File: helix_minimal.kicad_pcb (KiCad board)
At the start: 2 copper layers, 50 x 50 mm, 20 parts, among them J1 USB-C, J4 sd card, J5 SWD, J6 pico hdmi, U1 STM32C071FBP6, U2 AP2112K-3.3, U3 WIZ850io

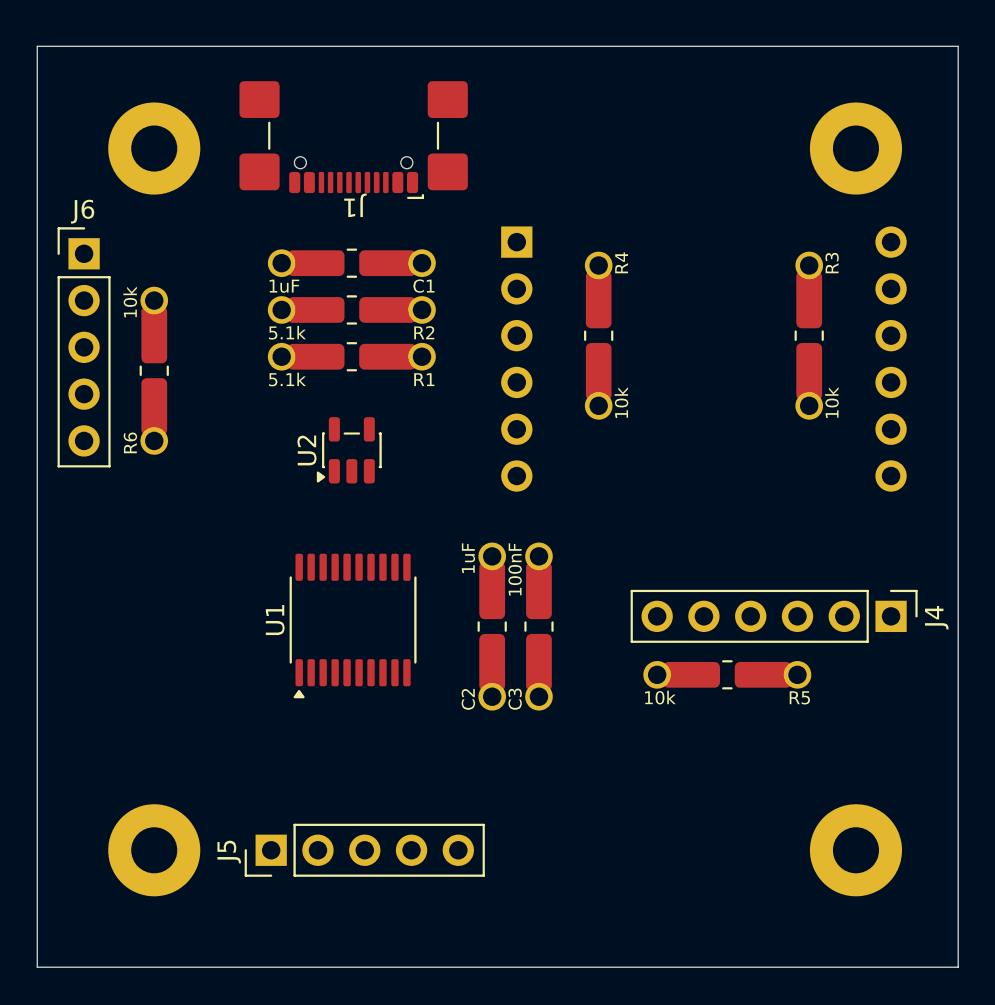
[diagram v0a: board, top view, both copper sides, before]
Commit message: Route PCB with fixed fine-pitch rules
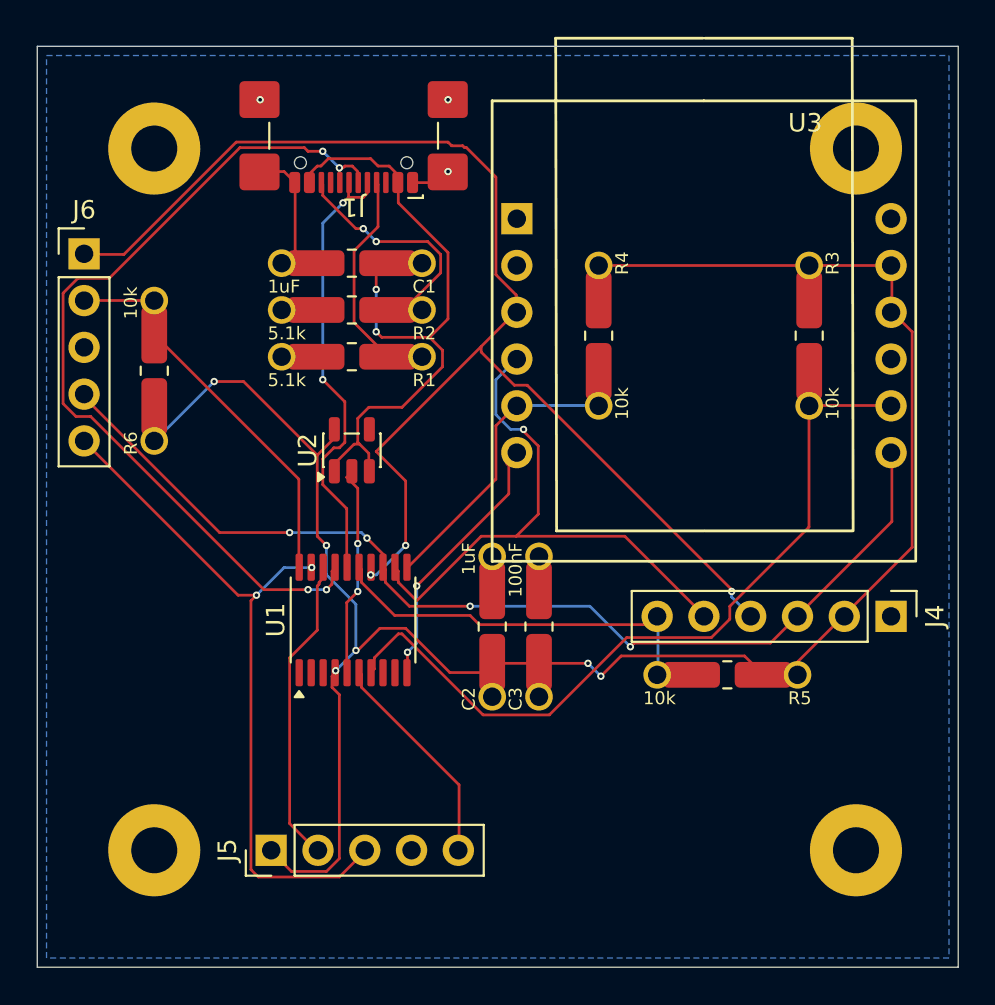
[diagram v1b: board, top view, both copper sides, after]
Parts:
- moved U3 1.27 mm to (137.8, 73.7)
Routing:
- net +3V3: track 0.00 -> 107.7 mm, vias 0 -> 6
- net /SPI_MOSI: track 0.00 -> 73.9 mm, vias 0 -> 3
- net /SPI_MISO: track 0.00 -> 57.0 mm, vias 0 -> 4
- net /USB_DP: track 0.00 -> 46.5 mm, vias 0 -> 4
- net /WIZ_RST: track 0.00 -> 42.6 mm
- net /SWCLK: track 0.00 -> 38.5 mm, vias 0 -> 2
- net VBUS: track 0.00 -> 36.5 mm, vias 0 -> 2
- net /SPI_SCK: track 0.00 -> 33.0 mm, vias 0 -> 1
- net /USB_DM: track 0.00 -> 24.9 mm, vias 0 -> 2
- net /SD_CS: track 0.00 -> 21.3 mm
- net GND: track 0.00 -> 20.8 mm, vias 0 -> 5
- net /PICO_CS: track 0.00 -> 19.8 mm
- net /SWDIO: track 0.00 -> 16.0 mm
- net /WIZ_CS: track 0.00 -> 15.8 mm
- net /WIZ_INT: track 0.00 -> 14.3 mm, vias 0 -> 2
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- added copper zone on B.Cu, net GND

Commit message: Reroute PCB without in-pad vias and widen copper
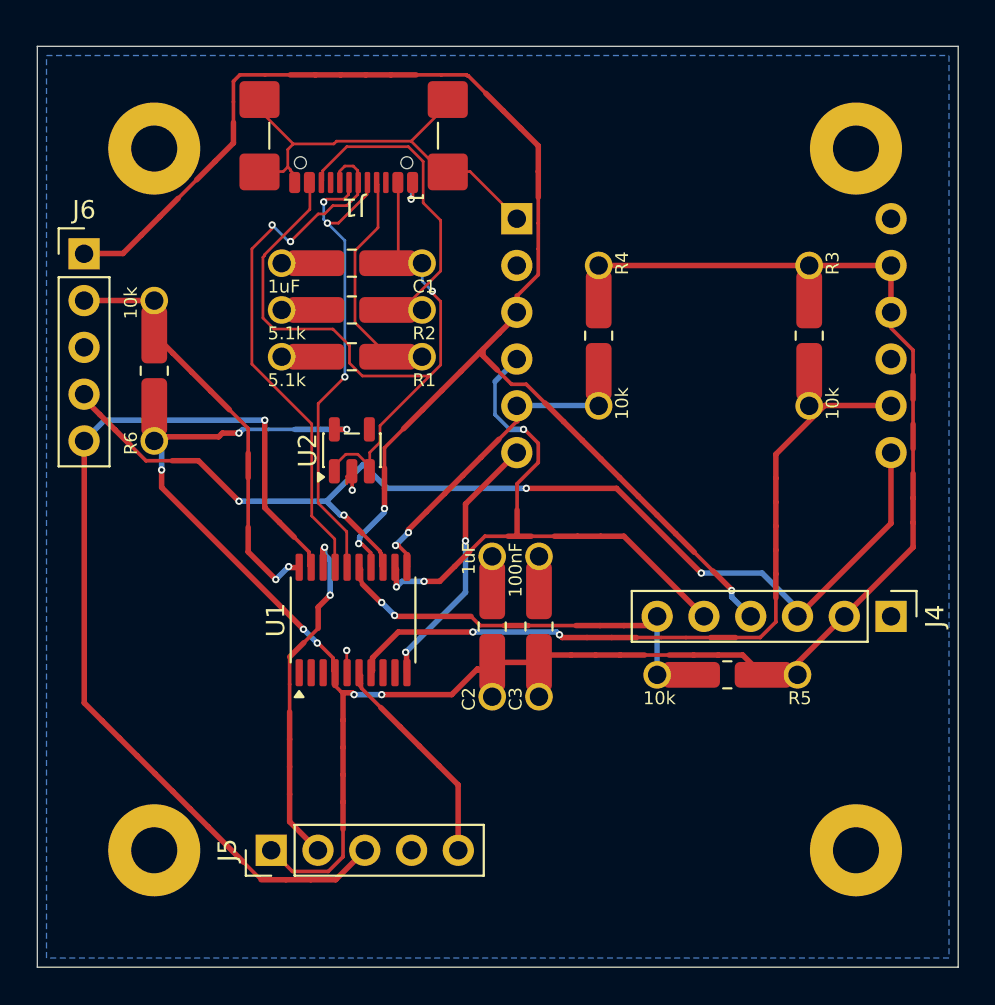
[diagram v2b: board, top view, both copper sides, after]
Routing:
- net /USB_DP: track 46.5 -> 29.4 mm, vias 4 -> 2
- net /SWCLK: track 38.5 -> 53.4 mm, vias 2 -> 1
- net GND: track 20.8 -> 29.6 mm, vias 5 -> 3
- net /SPI_MOSI: track 73.9 -> 80.0 mm
- net VBUS: track 36.5 -> 41.6 mm, vias 2 -> 1
- net /SPI_MISO: track 57.0 -> 61.1 mm
- net /CC2: track 13.3 -> 17.1 mm, vias 2 -> 0
- net /SWDIO: track 16.0 -> 19.3 mm, vias 0 -> 2
- net /USB_DM: track 24.9 -> 27.2 mm, vias 2 -> 3
- net /WIZ_RST: track 42.6 -> 40.9 mm, vias 0 -> 2
- net /PICO_CS: track 19.8 -> 21.3 mm, vias 0 -> 2
- net /WIZ_CS: track 15.8 -> 16.4 mm, vias 0 -> 2
- net /SPI_SCK: track 33.0 -> 32.7 mm, vias 1 -> 3
- net /SD_CS: track 21.3 -> 21.2 mm, vias 0 -> 2
- net +3V3: track 107.7 -> 107.5 mm, vias 6 -> 7

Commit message: Reroute board with hard 0.30 mm ordinary traces
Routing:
- net GND: track 29.6 -> 181.3 mm, vias 3 -> 7
- net /SWCLK: track 53.4 -> 32.9 mm, vias 1 -> 0
- net VBUS: track 41.6 -> 30.4 mm
- net /SPI_MOSI: track 80.0 -> 68.9 mm, vias 3 -> 2
- net /SWDIO: track 19.3 -> 29.7 mm, vias 2 -> 0
- net /USB_DM: track 27.2 -> 34.2 mm
- net /CC2: track 17.1 -> 10.6 mm, vias 0 -> 2
- net /WIZ_RST: track 40.9 -> 35.1 mm
- net +3V3: track 107.5 -> 104.3 mm, vias 7 -> 5
- net /SPI_SCK: track 32.7 -> 34.8 mm, vias 3 -> 0
- net /USB_DP: track 29.4 -> 27.5 mm
- net /SPI_MISO: track 61.1 -> 62.6 mm, vias 4 -> 7
- net /PICO_CS: track 21.3 -> 20.1 mm, vias 2 -> 0
- net /SD_CS: track 21.2 -> 21.9 mm, vias 2 -> 1
- net /WIZ_CS: track 16.4 -> 15.7 mm, vias 2 -> 0
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
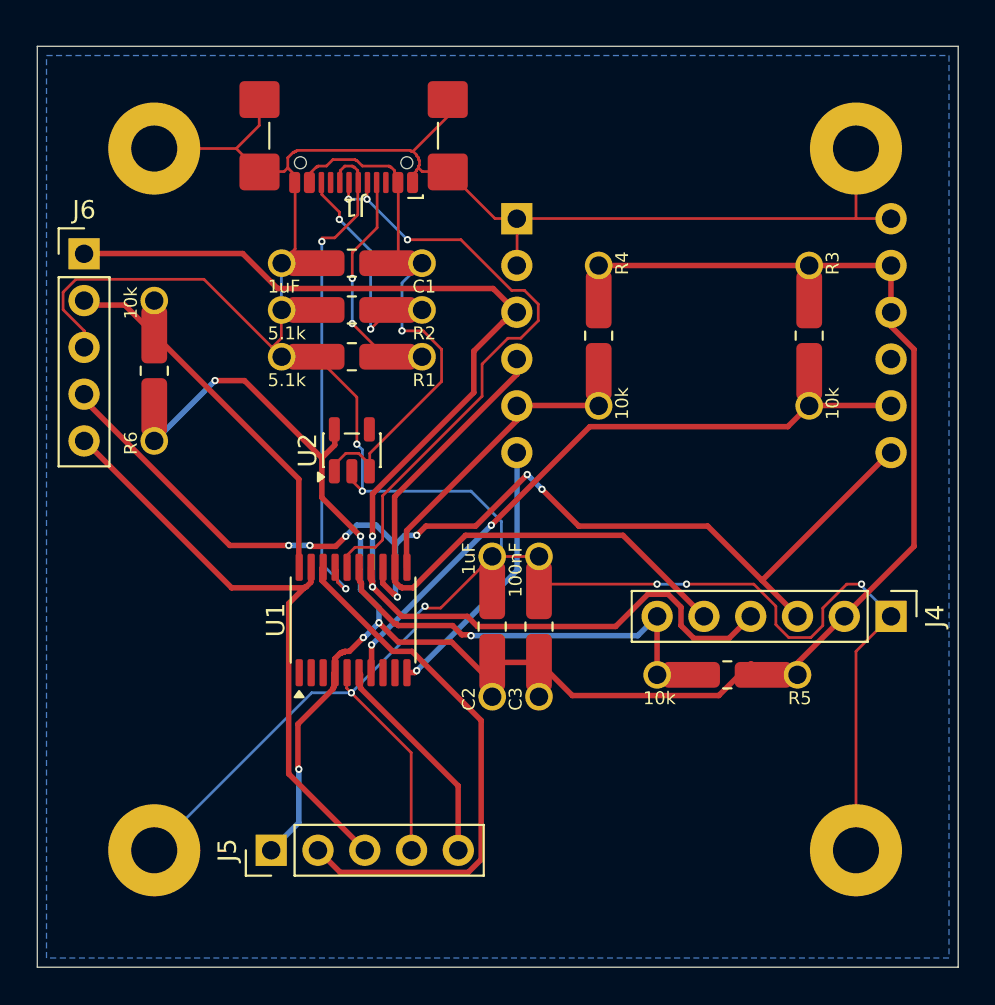
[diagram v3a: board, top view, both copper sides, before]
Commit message: Use dual ground pours and route signals with higher via cost
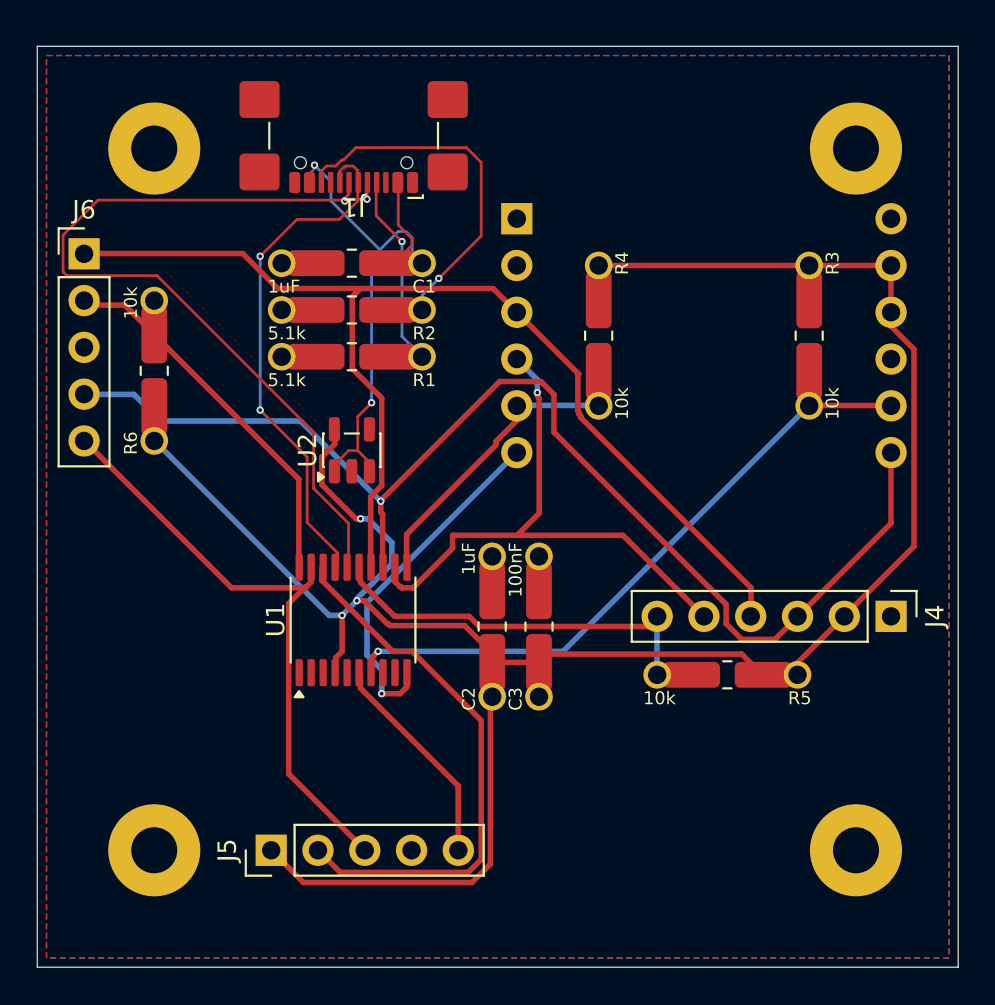
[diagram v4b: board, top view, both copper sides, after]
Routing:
- net GND: track 181.3 -> 0.00 mm, vias 7 -> 0
- net +3V3: track 104.3 -> 120.6 mm, vias 5 -> 3
- net /USB_DM: track 34.2 -> 46.8 mm, vias 3 -> 2
- net /CC2: track 10.6 -> 21.4 mm, vias 2 -> 1
- net /SPI_MOSI: track 68.9 -> 62.9 mm, vias 2 -> 0
- net /WIZ_INT: track 14.7 -> 19.1 mm
- net /SPI_MISO: track 62.6 -> 66.6 mm, vias 7 -> 1
- net /SPI_SCK: track 34.8 -> 31.5 mm, vias 0 -> 1
- net VBUS: track 30.4 -> 32.5 mm, vias 1 -> 2
- net /CC1: track 11.0 -> 12.4 mm, vias 2 -> 1
- net /USB_DP: track 27.5 -> 28.1 mm
- net /SD_CS: track 21.9 -> 21.4 mm, vias 1 -> 0
- net /WIZ_RST: track 35.1 -> 34.7 mm, vias 2 -> 1
- added copper zone on F.Cu, net GND

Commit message: Increase router turn penalty and reroute signal copper
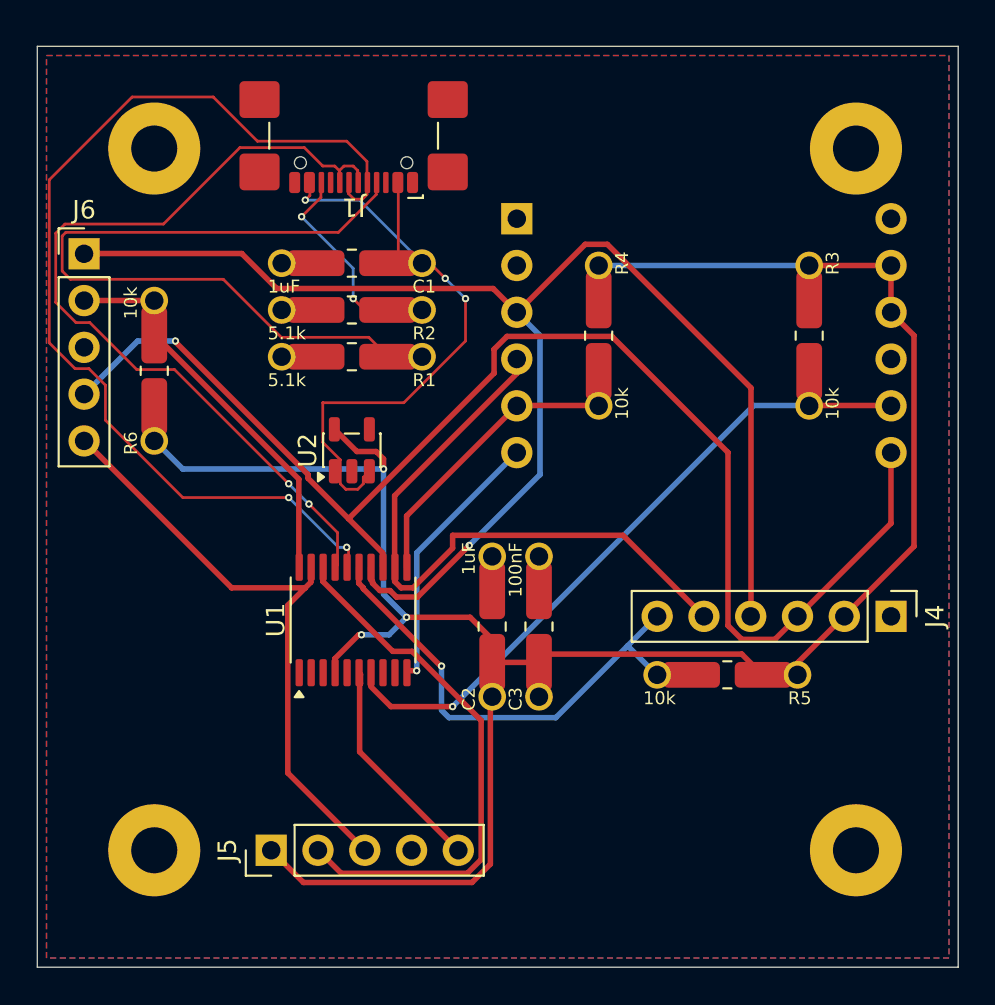
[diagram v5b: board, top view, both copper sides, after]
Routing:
- net /CC1: track 12.4 -> 40.2 mm, vias 1 -> 0
- net /USB_DP: track 28.1 -> 46.6 mm
- net /SPI_MOSI: track 62.9 -> 77.1 mm, vias 0 -> 1
- net /CC2: track 21.4 -> 10.1 mm, vias 1 -> 2
- net /SPI_MISO: track 66.6 -> 76.2 mm
- net /USB_DM: track 46.8 -> 56.1 mm
- net VBUS: track 32.5 -> 37.2 mm, vias 2 -> 3
- net /SD_CS: track 21.4 -> 26.0 mm, vias 0 -> 1
- net /WIZ_INT: track 19.1 -> 14.7 mm
- net /SPI_SCK: track 31.5 -> 35.2 mm, vias 1 -> 0
- net +3V3: track 120.6 -> 118.2 mm
- net /WIZ_RST: track 34.7 -> 35.5 mm

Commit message: Route USB signals first and retain project rules
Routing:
- net /CC1: track 40.2 -> 10.8 mm
- net /USB_DM: track 56.1 -> 33.8 mm, vias 2 -> 0
- net /SPI_MISO: track 76.2 -> 57.6 mm, vias 1 -> 3
- net /CC2: track 10.1 -> 25.7 mm, vias 2 -> 0
- net +3V3: track 118.2 -> 131.7 mm, vias 3 -> 2
- net /USB_DP: track 46.6 -> 34.7 mm, vias 2 -> 0
- net VBUS: track 37.2 -> 31.1 mm, vias 3 -> 1
- net /SPI_MOSI: track 77.1 -> 81.1 mm, vias 1 -> 0
- net /SWCLK: track 32.9 -> 32.2 mm, vias 0 -> 1
